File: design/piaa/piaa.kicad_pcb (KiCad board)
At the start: 2 copper layers, 98.6 x 53.8 mm, 104 parts, among them J1 Screw_Terminal_01x03, J2 Conn_02x04_Counter_Clockwise, J6 Screw_Terminal_01x06, J7 Screw_Terminal_01x05, J8 Screw_Terminal_01x02, J9 Conn_01x06_Female, P1 PS2805-4, Q1 FQT13N06L, Q2 FQT13N06L, Q3 FQT13N06L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

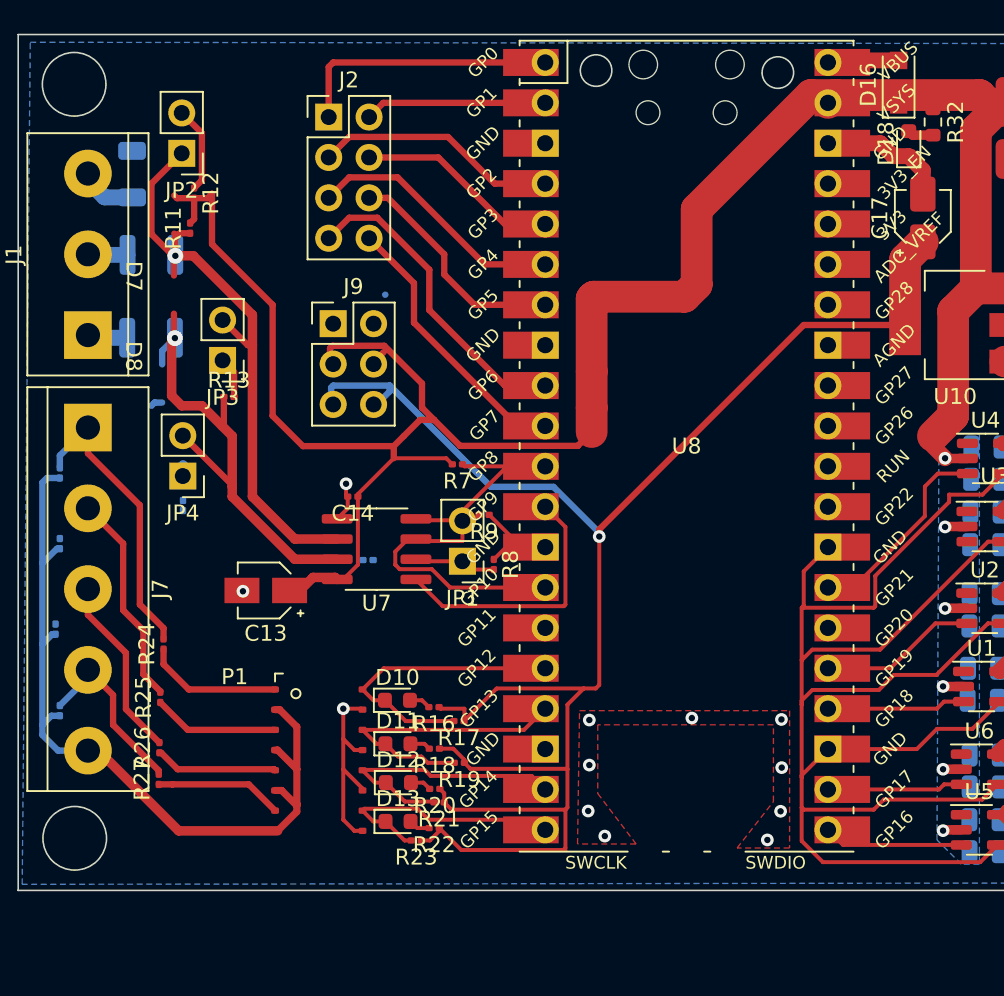
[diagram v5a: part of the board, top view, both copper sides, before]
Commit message: thicker 3v3 line
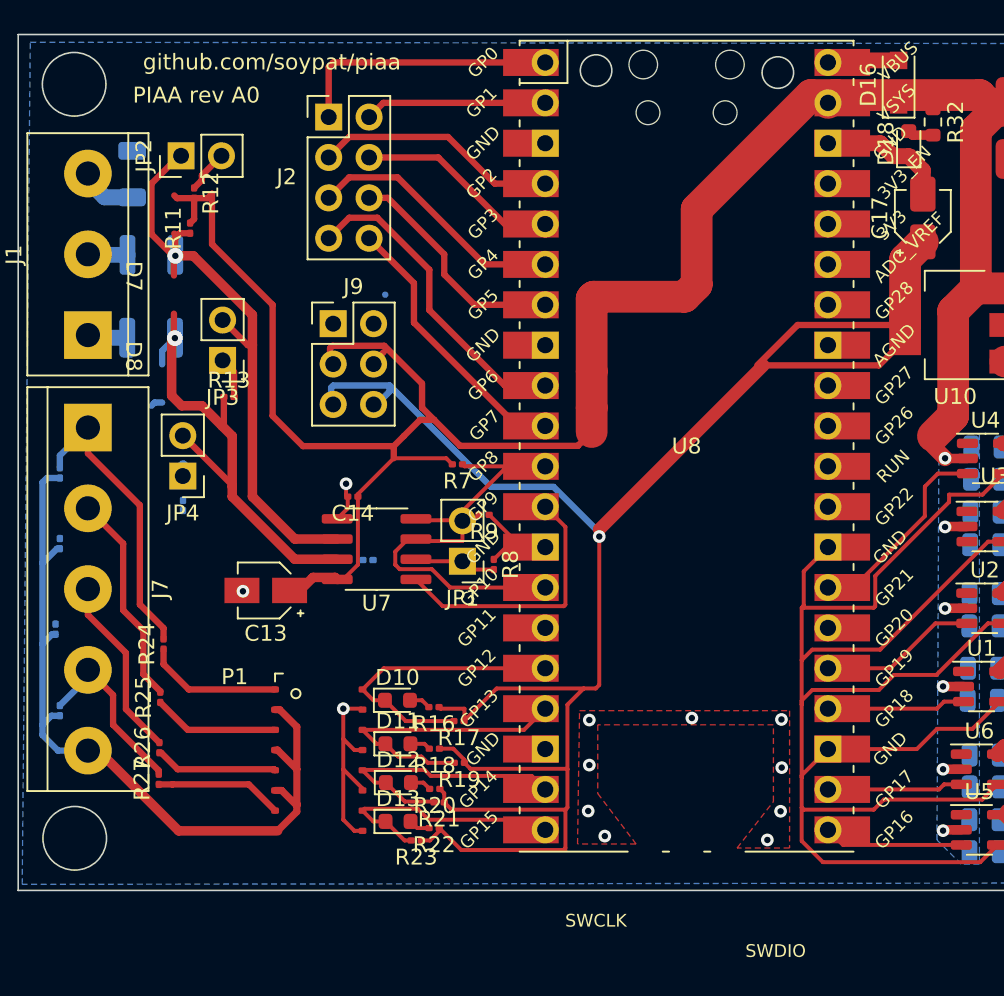
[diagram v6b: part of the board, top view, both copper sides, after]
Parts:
- moved JP2 0.16 mm to (116.8, 85.9), turned to 90 degrees
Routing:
- net +3V3: track 114.6 -> 125.5 mm
- net Net-(JP2-Pad2): track 5.45 -> 2.74 mm
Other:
- board text added: "PIAA rev A0"
- board text added: "github.com/soypat/piaa"
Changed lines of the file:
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@@
       (effects (font (size 0.8 0.8) (thickness 0.15)))
     )
-    (fp_text user "SWCLK" (at -5.7 26.2) (layer "F.SilkS")
+    (fp_text user "SWCLK" (at -5.7 29.845) (layer "F.SilkS")
       (effects (font (size 0.8 0.8) (thickness 0.15)))
     )
@@
       (effects (font (size 0.8 0.8) (thickness 0.15)))
     )
-    (fp_text user "SWDIO" (at 5.6 26.2) (layer "F.SilkS")
+    (fp_text user "SWDIO" (at 5.6 31.75) (layer "F.SilkS")
       (effects (font (size 0.8 0.8) (thickness 0.15)))
     )
@@
     (property "Sheetname" "")
     (attr through_hole)
-    (fp_text reference "J2" (at 1.27 -2.33) (layer "F.SilkS")
+    (fp_text reference "J2" (at -2.647597 3.760345) (layer "F.SilkS")
       (effects (font (size 1 1) (thickness 0.15)))
     )
@@
   )
   (footprint "Connector_PinHeader_2.54mm:PinHeader_1x02_P2.54mm_Vertical" (layer "F.Cu")
-    (at 116.84 85.725 180)
+    (at 116.798565 85.881042 90)
     (descr "Through hole straight pin header, 1x02, 2.54mm pitch, single row")
     (tags "Through hole pin header THT 1x02 2.54mm single row")
@@
     (property "Sheetname" "")
     (attr through_hole)
-    (fp_text reference "JP2" (at 0 -2.33) (layer "F.SilkS")
+    (fp_text reference "JP2" (at 0 -2.33 90) (layer "F.SilkS")
       (effects (font (size 1 1) (thickness 0.15)))
     )
-    (fp_text value "jumper" (at 0 4.87) (layer "F.Fab")
+    (fp_text value "jumper" (at 0 4.87 90) (layer "F.Fab")
       (effects (font (size 1 1) (thickness 0.15)))
     )
-    (fp_text user "${REFERENCE}" (at 0 1.27 90) (layer "F.Fab")
+    (fp_text user "${REFERENCE}" (at 0 1.27) (layer "F.Fab")
       (effects (font (size 1 1) (thickness 0.15)))
     )
@@
     (fp_line (start -1.27 -0.635) (end -0.635 -1.27) (layer "F.Fab") (width 0.1))
     (fp_line (start 1.27 -1.27) (end 1.27 3.81) (layer "F.Fab") (width 0.1))
-    (pad "1" thru_hole rect (at 0 0 180) (size 1.7 1.7) (drill 1) (layers *.Cu *.Mask)
+    (pad "1" thru_hole rect (at 0 0 90) (size 1.7 1.7) (drill 1) (layers *.Cu *.Mask)
       (net 11 "Net-(D7-Pad2)") (pinfunction "A") (pintype "passive"))
-    (pad "2" thru_hole oval (at 0 2.54 180) (size 1.7 1.7) (drill 1) (layers *.Cu *.Mask)
+    (pad "2" thru_hole oval (at 0 2.54 90) (size 1.7 1.7) (drill 1) (layers *.Cu *.Mask)
       (net 54 "Net-(JP2-Pad2)") (pinfunction "B") (pintype "passive"))
     (model "${KICAD6_3DMODEL_DIR}/Connector_PinHeader_2.54mm.3dshapes/PinHeader_1x02_P2.54mm_Vertical.wrl"
@@
   (gr_circle (center 154.329099 80.645) (end 154.964099 81.407) (layer "Edge.Cuts") (width 0.1) (fill none))
   (gr_circle (center 110.075125 81.382191) (end 112.075125 81.382191) (layer "Edge.Cuts") (width 0.1) (fill none))
+  (gr_text "PIAA rev A0" (at 117.762341 82.068342) (layer "F.SilkS")
+    (effects (font (size 1 1) (thickness 0.25)))
+  )
+  (gr_text "github.com/soypat/piaa" (at 122.511095 79.987572) (layer "F.SilkS")
+    (effects (font (size 1 1) (thickness 0.25)))
+  )
   (gr_text "CYW43439\n+\nProant\nKeepout" (at 148.59 125.603) (layer "Edge.Cuts")
     (effects (font (size 1 1) (thickness 0.15)))
@@
   (segment (start 190.233611 87.614544) (end 189.006264 86.387197) (width 2) (layer "F.Cu") (net 3))
   (segment (start 192.817873 87.614544) (end 190.233611 87.614544) (width 2) (layer "F.Cu") (net 3))
+  (segment (start 143.097489 109.378511) (end 143.097489 109.823489) (width 0.4) (layer "F.Cu") (net 4))
   (segment (start 142.113 119.38) (end 141.097 120.396) (width 0.25) (layer "F.Cu") (net 4))
   (segment (start 133.072266 125.694186) (end 133.348996 125.970916) (width 0.25) (layer "F.Cu") (net 4))
-  (segment (start 143.097489 109.378511) (end 155.956 96.52) (width 0.4) (layer "F.Cu") (net 4))
   (segment (start 142.113 119.38) (end 142.875 119.38) (width 0.25) (layer "F.Cu") (net 4))
   (segment (start 134.416428 129.54) (end 140.843 129.54) (width 0.25) (layer "F.Cu") (net 4))
   (segment (start 143.097489 109.823489) (end 143.097489 119.157511) (width 0.25) (layer "F.Cu") (net 4))
+  (segment (start 162.331 97.42) (end 160.691 99.06) (width 0.4) (layer "F.Cu") (net 4))
   (segment (start 131.907307 128.939591) (end 132.444342 128.939591) (width 0.25) (layer "F.Cu") (net 4))
   (segment (start 134.62 121.405901) (end 134.595 121.430901) (width 0.25) (layer "F.Cu") (net 4))
+  (segment (start 153.416 99.06) (end 143.097489 109.378511) (width 0.8) (layer "F.Cu") (net 4))
   (segment (start 133.348996 125.970916) (end 133.348996 126.544332) (width 0.25) (layer "F.Cu") (net 4))
+  (segment (start 162.331 96.52) (end 155.575 96.52) (width 0.4) (layer "F.Cu") (net 4))
   (segment (start 132.444342 128.939591) (end 133.035 128.348933) (width 0.25) (layer "F.Cu") (net 4))
   (segment (start 141.097 120.396) (end 141.097 124.46) (width 0.25) (layer "F.Cu") (net 4))
   (segment (start 141.097 126.873) (end 140.97 127) (width 0.25) (layer "F.Cu") (net 4))
+  (segment (start 155.575 96.52) (end 153.035 99.06) (width 0.4) (layer "F.Cu") (net 4))
   (segment (start 141.06748 124.43048) (end 134.994162 124.43048) (width 0.25) (layer "F.Cu") (net 4))
   (segment (start 133.118954 120.65) (end 134.62 120.65) (width 0.25) (layer "F.Cu") (net 4))
   (segment (start 134.618996 124.055314) (end 134.994162 124.43048) (width 0.25) (layer "F.Cu") (net 4))
   (segment (start 133.920021 123.165978) (end 133.048726 123.165978) (width 0.25) (layer "F.Cu") (net 4))
+  (segment (start 162.331 96.52) (end 162.331 97.42) (width 0.4) (layer "F.Cu") (net 4))
   (segment (start 134.595 121.430901) (end 136.645901 119.38) (width 0.25) (layer "F.Cu") (net 4))
   (segment (start 140.843 129.54) (end 140.97 129.54) (width 0.25) (layer "F.Cu") (net 4))
   (segment (start 141.097 124.46) (end 141.06748 124.43048) (width 0.25) (layer "F.Cu") (net 4))
-  (segment (start 143.097489 109.823489) (end 143.097489 109.378511) (width 0.4) (layer "F.Cu") (net 4))
   (segment (start 134.618996 123.864953) (end 133.920021 123.165978) (width 0.25) (layer "F.Cu") (net 4))
   (segment (start 136.645901 119.38) (end 142.113 119.38) (width 0.25) (layer "F.Cu") (net 4))
@@
   (segment (start 133.035 128.348933) (end 133.035 128.158572) (width 0.25) (layer "F.Cu") (net 4))
   (segment (start 133.035 128.158572) (end 134.416428 129.54) (width 0.25) (layer "F.Cu") (net 4))
+  (segment (start 160.691 99.06) (end 153.416 99.06) (width 0.4) (layer "F.Cu") (net 4))
   (segment (start 140.97 129.413) (end 140.97 127) (width 0.25) (layer "F.Cu") (net 4))
   (segment (start 162.331 96.52) (end 162.331 92.407) (width 2) (layer "F.Cu") (net 4))
@@
   (segment (start 141.097 124.46) (end 141.097 126.873) (width 0.25) (layer "F.Cu") (net 4))
   (segment (start 134.62 120.65) (end 134.62 121.405901) (width 0.25) (layer "F.Cu") (net 4))
-  (segment (start 155.956 96.52) (end 162.331 96.52) (width 0.4) (layer "F.Cu") (net 4))
   (via (at 143.097489 109.823489) (size 0.8) (drill 0.4) (layers "F.Cu" "B.Cu") (net 4))
   (segment (start 136.291489 106.700489) (end 129.921 100.33) (width 0.4) (layer "B.Cu") (net 4))
@@
   (segment (start 134.493 109.499) (end 135.534 108.458) (width 0.25) (layer "F.Cu") (net 53))
   (segment (start 139.7 105.41) (end 134.625 105.41) (width 0.25) (layer "F.Cu") (net 53))
-  (segment (start 118.11 87.415411) (end 118.11 84.455) (width 0.4) (layer "F.Cu") (net 54))
-  (segment (start 118.11 84.455) (end 116.84 83.185) (width 0.4) (layer "F.Cu") (net 54))
+  (segment (start 118.11 87.109607) (end 119.338565 85.881042) (width 0.4) (layer "F.Cu") (net 54))
+  (segment (start 118.11 87.415411) (end 118.11 87.109607) (width 0.4) (layer "F.Cu") (net 54))
   (segment (start 117.620279 87.905132) (end 118.11 87.415411) (width 0.4) (layer "F.Cu") (net 54))
   (segment (start 120.130563 99.469618) (end 119.408704 98.747759) (width 0.4) (layer "F.Cu") (net 55))
